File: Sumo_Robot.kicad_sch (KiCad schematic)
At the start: 0 parts

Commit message: updated poer and range sensor scheamtics
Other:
- sheet RangeSensors ports: added SCL, SDA; removed none
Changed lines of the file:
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@@
 	(paper "A4")
 	(sheet
-		(at 39.37 154.94)
+		(at 35.56 176.53)
 		(size 22.86 15.24)
 		(exclude_from_sim no)
@@
 		)
 		(property "Sheetname" "Mechanical"
-			(at 39.37 154.2284 0)
+			(at 35.56 175.8184 0)
 			(effects
 				(font
@@
 		)
 		(property "Sheetfile" "mechanical.kicad_sch"
-			(at 39.37 170.7646 0)
+			(at 35.56 192.3546 0)
 			(effects
 				(font
@@
 	)
 	(sheet
-		(at 223.52 27.94)
+		(at 38.1 137.16)
 		(size 24.13 17.78)
 		(exclude_from_sim no)
@@
 		)
 		(property "Sheetname" "InfraredReceiver"
-			(at 223.52 27.2284 0)
+			(at 38.1 136.4484 0)
 			(effects
 				(font
@@
 		)
 		(property "Sheetfile" "receiver.kicad_sch"
-			(at 223.52 46.3046 0)
+			(at 38.1 155.5246 0)
 			(effects
 				(font
@@
 	)
 	(sheet
-		(at 35.56 68.58)
+		(at 33.02 60.96)
 		(size 27.94 20.32)
 		(exclude_from_sim no)
@@
 		)
 		(property "Sheetname" "RangeSensors"
-			(at 35.56 67.8684 0)
+			(at 33.02 60.2484 0)
 			(effects
 				(font
@@
 		)
 		(property "Sheetfile" "range.kicad_sch"
-			(at 35.56 89.4846 0)
-			(effects
-				(font
-					(size 1.27 1.27)
-				)
-				(justify left top)
-			)
-		)
+			(at 33.02 81.8646 0)
+			(effects
+				(font
+					(size 1.27 1.27)
+				)
+				(justify left top)
+			)
+		)
+		(pin "SCL" input
+			(at 60.96 67.31 0)
+			(effects
+				(font
+					(size 1.27 1.27)
+				)
+				(justify right)
+			)
+		)
+		(pin "SDA" input
+			(at 60.96 73.66 0)
+			(effects
+				(font
+					(size 1.27 1.27)
+				)
+				(justify right)
+			)
+		)

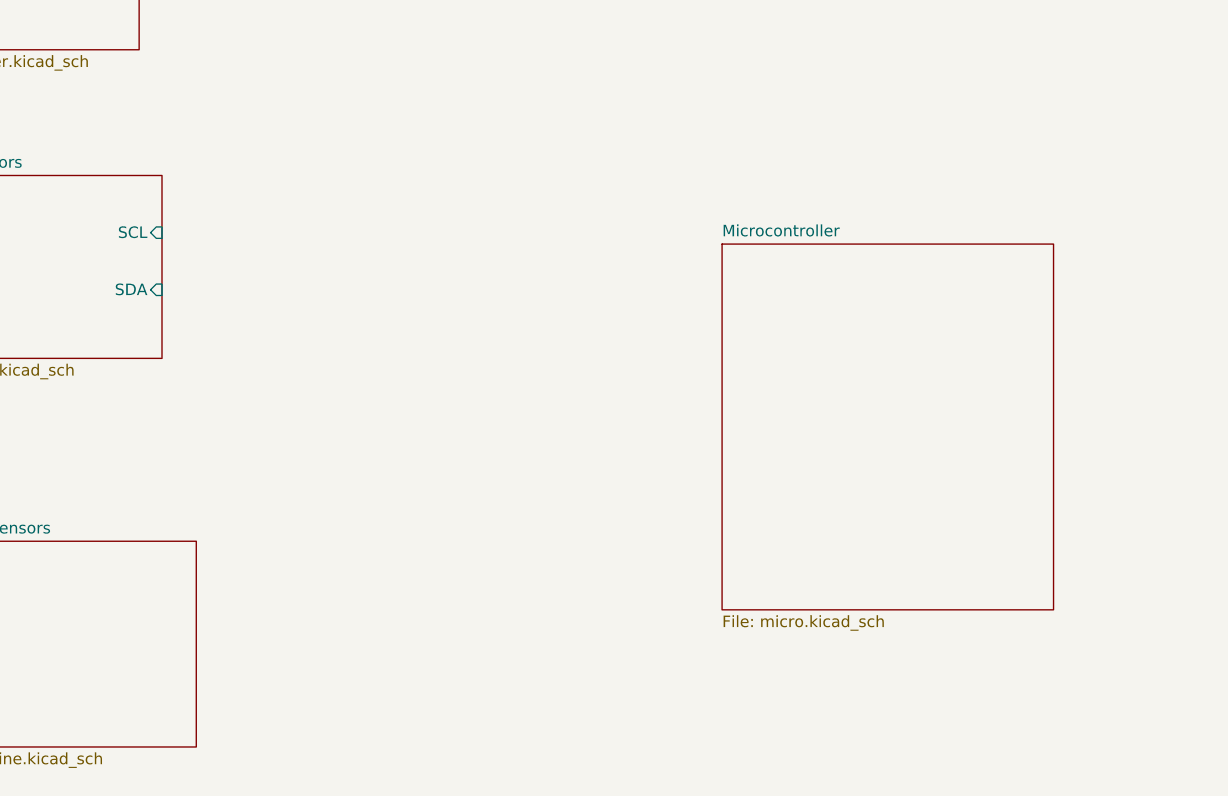
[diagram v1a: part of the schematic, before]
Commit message: added I2C lines
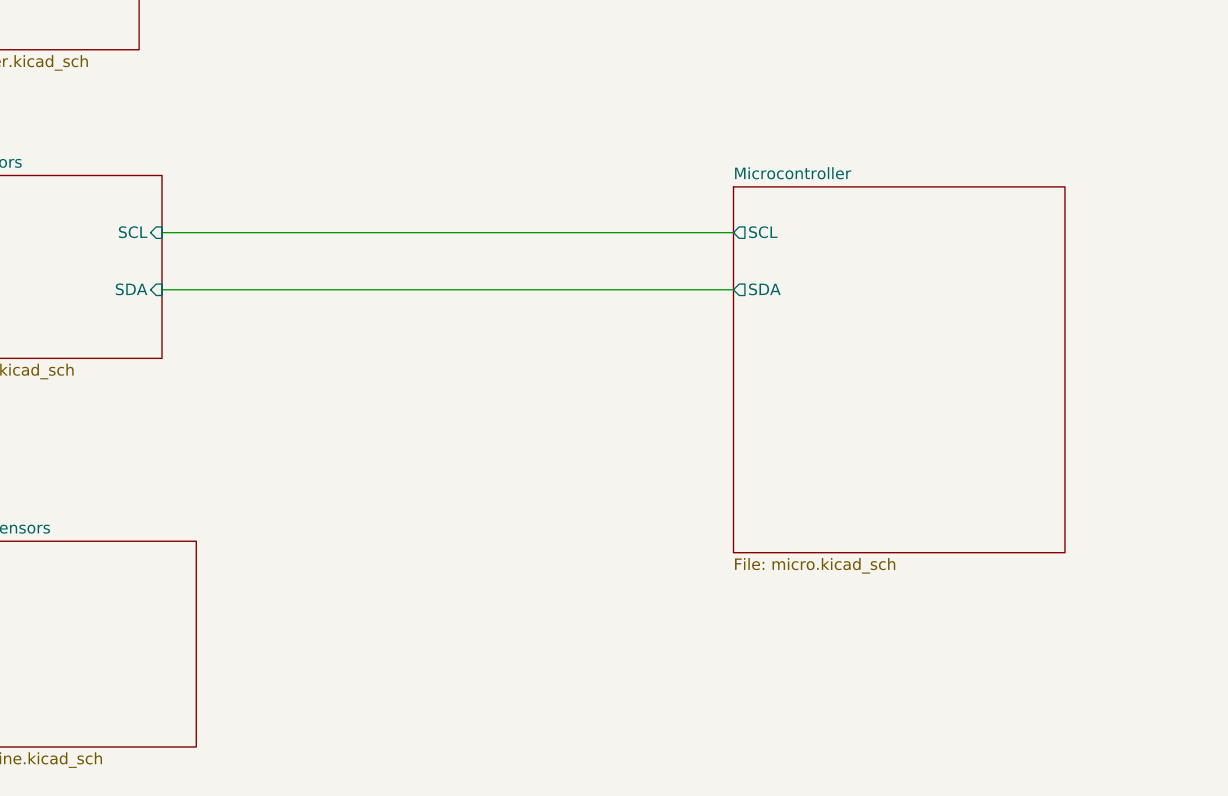
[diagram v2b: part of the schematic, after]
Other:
- sheet Microcontroller ports: added SCL, SDA; removed none
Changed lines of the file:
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@@
 	(generator_version "9.0")
 	(paper "A4")
+	(wire
+		(pts
+			(xy 60.96 67.31) (xy 124.46 67.31)
+		)
+		(stroke
+			(width 0)
+			(type default)
+		)
+	)
+	(wire
+		(pts
+			(xy 60.96 73.66) (xy 124.46 73.66)
+		)
+		(stroke
+			(width 0)
+			(type default)
+		)
+	)
 	(sheet
 		(at 35.56 176.53)
@@
 	)
 	(sheet
-		(at 123.19 68.58)
+		(at 124.46 62.23)
 		(size 36.83 40.64)
 		(exclude_from_sim no)
@@
 		)
 		(property "Sheetname" "Microcontroller"
-			(at 123.19 67.8684 0)
+			(at 124.46 61.5184 0)
 			(effects
 				(font
@@
 		)
 		(property "Sheetfile" "micro.kicad_sch"
-			(at 123.19 109.8046 0)
-			(effects
-				(font
-					(size 1.27 1.27)
-				)
-				(justify left top)
-			)
-		)
+			(at 124.46 103.4546 0)
+			(effects
+				(font
+					(size 1.27 1.27)
+				)
+				(justify left top)
+			)
+		)
+		(pin "SCL" output
+			(at 124.46 67.31 180)
+			(effects
+				(font
+					(size 1.27 1.27)
+				)
+				(justify left)
+			)
+		)
+		(pin "SDA" output
+			(at 124.46 73.66 180)
+			(effects
+				(font
+					(size 1.27 1.27)
+				)
+				(justify left)
+			)
+		)

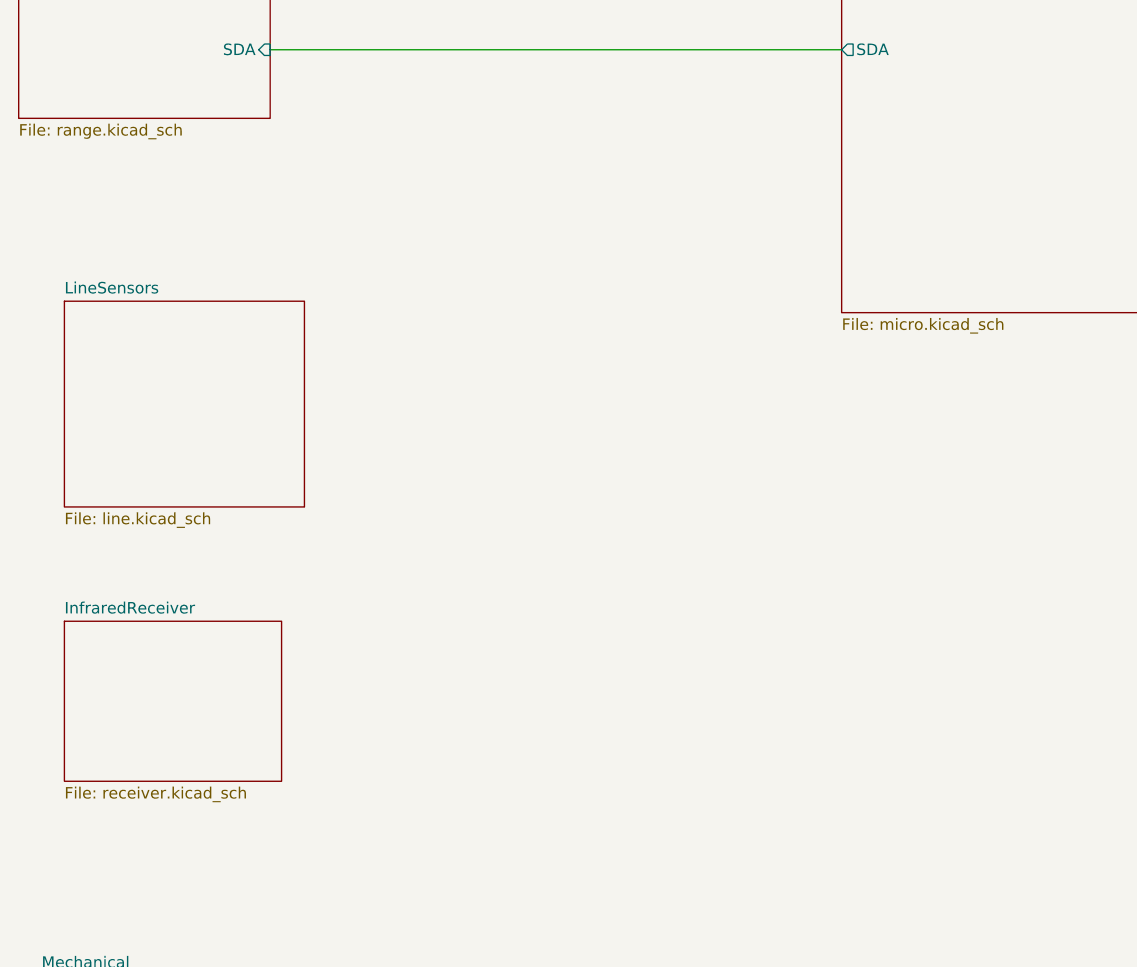
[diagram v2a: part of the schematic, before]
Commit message: added IR receiver circuit
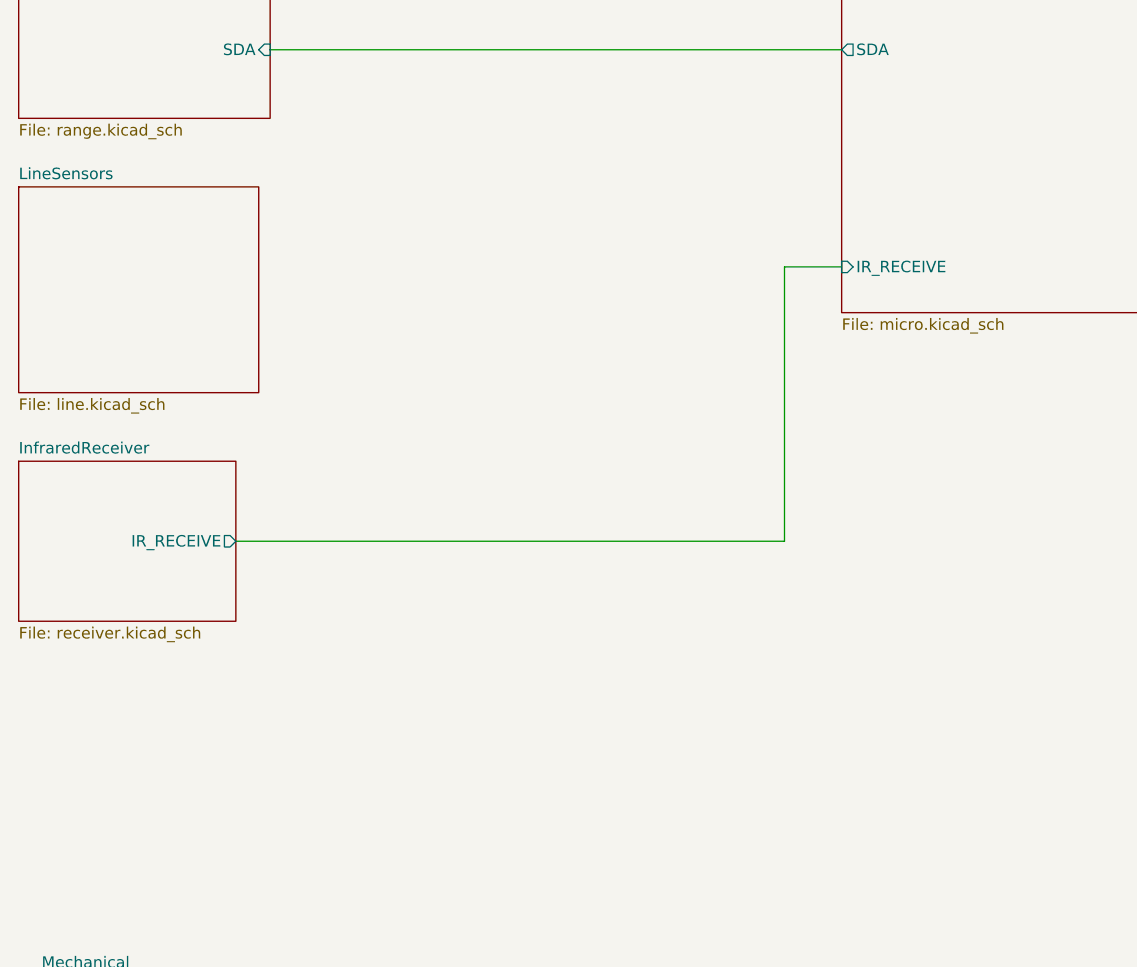
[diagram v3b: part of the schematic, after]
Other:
- sheet InfraredReceiver ports: added IR_RECEIVE; removed none
- sheet Microcontroller ports: added IR_RECEIVE; removed none
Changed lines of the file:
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@@
+	(wire
+		(pts
+			(xy 118.11 128.27) (xy 118.11 97.79)
+		)
+		(stroke
+			(width 0)
+			(type default)
+		)
+	)
+	(wire
+		(pts
+			(xy 57.15 128.27) (xy 118.11 128.27)
+		)
+		(stroke
+			(width 0)
+			(type default)
+		)
+	)
 	(wire
 		(pts
@@
 		)
 	)
+	(wire
+		(pts
+			(xy 118.11 97.79) (xy 124.46 97.79)
+		)
+		(stroke
+			(width 0)
+			(type default)
+		)
+	)
 	(sheet
 		(at 35.56 176.53)
@@
 	)
 	(sheet
-		(at 38.1 137.16)
+		(at 33.02 119.38)
 		(size 24.13 17.78)
 		(exclude_from_sim no)
@@
 		)
 		(property "Sheetname" "InfraredReceiver"
-			(at 38.1 136.4484 0)
+			(at 33.02 118.6684 0)
 			(effects
 				(font
@@
 		)
 		(property "Sheetfile" "receiver.kicad_sch"
-			(at 38.1 155.5246 0)
-			(effects
-				(font
-					(size 1.27 1.27)
-				)
-				(justify left top)
+			(at 33.02 137.7446 0)
+			(effects
+				(font
+					(size 1.27 1.27)
+				)
+				(justify left top)
+			)
+		)
+		(pin "IR_RECEIVE" output
+			(at 57.15 128.27 0)
+			(effects
+				(font
+					(size 1.27 1.27)
+				)
+				(justify right)
 			)
 		)
@@
 			)
 		)
+		(pin "IR_RECEIVE" input
+			(at 124.46 97.79 180)
+			(effects
+				(font
+					(size 1.27 1.27)
+				)
+				(justify left)
+			)
+		)
 		(instances
 			(project "Sumo_Robot"
@@
 	)
 	(sheet
-		(at 38.1 101.6)
+		(at 33.02 88.9)
 		(size 26.67 22.86)
 		(exclude_from_sim no)
@@
 		)
 		(property "Sheetname" "LineSensors"
-			(at 38.1 100.8884 0)
+			(at 33.02 88.1884 0)
 			(effects
 				(font
@@
 		)
 		(property "Sheetfile" "line.kicad_sch"
-			(at 38.1 125.0446 0)
-			(effects
-				(font
+			(at 33.02 112.3446 0)
+			(effects
+				(font

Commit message: added more details to schematics
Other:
- sheet LineSensors ports: added LD_BACK_LEFT, LD_BACK_RIGHT, LD_FRONT_LEFT, LD_FRONT_RIGHT; removed none
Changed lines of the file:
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@@
+			)
+		)
+		(pin "LD_FRONT_LEFT" output
+			(at 59.69 92.71 0)
+			(effects
+				(font
+					(size 1.27 1.27)
+				)
+				(justify right)
+			)
+		)
+		(pin "LD_BACK_RIGHT" output
+			(at 59.69 107.95 0)
+			(effects
+				(font
+					(size 1.27 1.27)
+				)
+				(justify right)
+			)
+		)
+		(pin "LD_BACK_LEFT" output
+			(at 59.69 102.87 0)
+			(effects
+				(font
+					(size 1.27 1.27)
+				)
+				(justify right)
+			)
+		)
+		(pin "LD_FRONT_RIGHT" output
+			(at 59.69 97.79 0)
+			(effects
+				(font
+					(size 1.27 1.27)
+				)
+				(justify right)
 			)
 		)

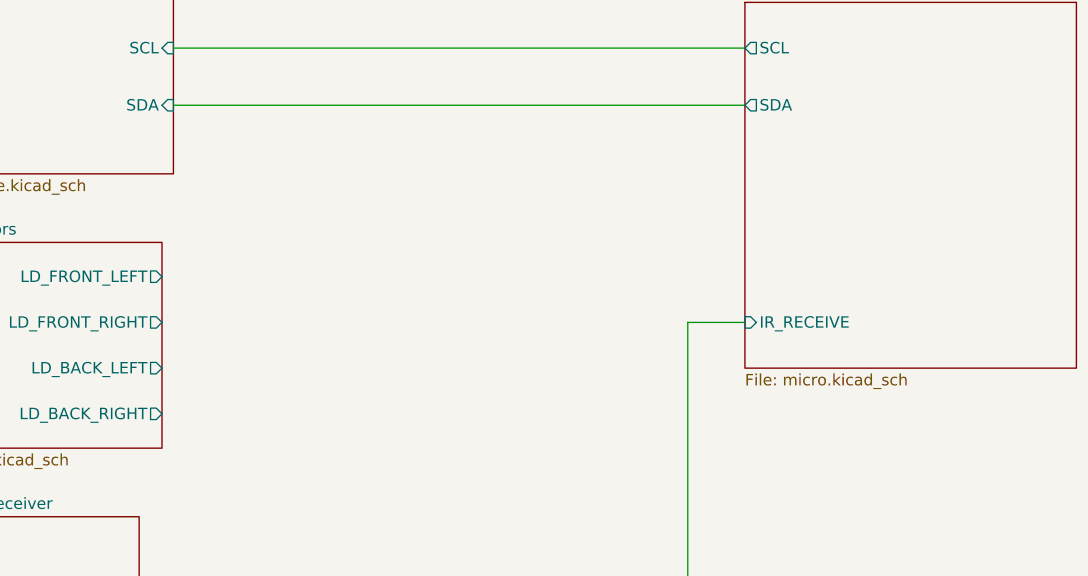
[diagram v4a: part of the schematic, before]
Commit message: updated logic for MCU
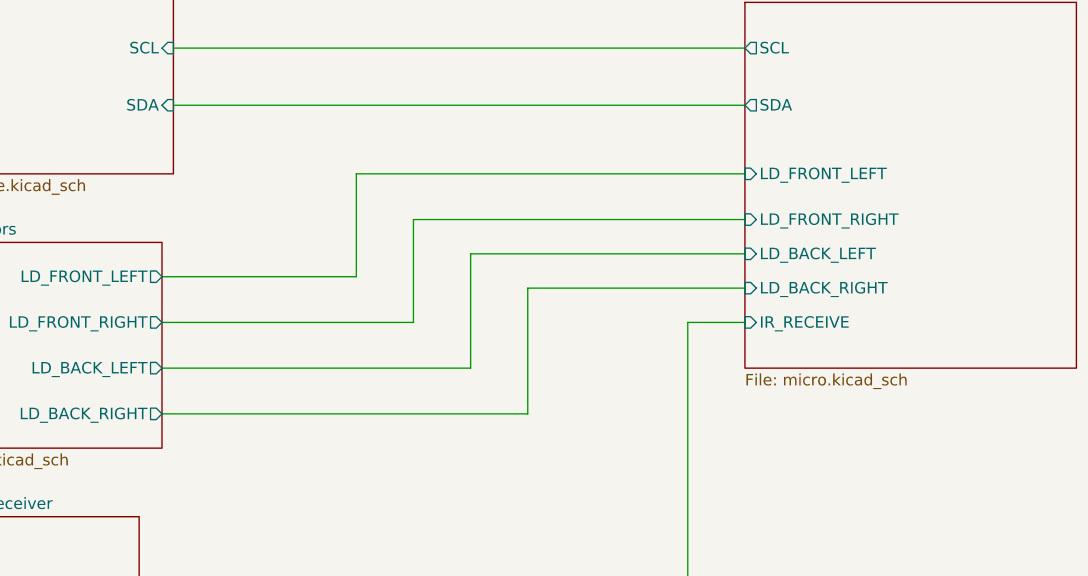
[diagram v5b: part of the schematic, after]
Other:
- sheet Microcontroller ports: added LD_BACK_LEFT, LD_BACK_RIGHT, LD_FRONT_LEFT, LD_FRONT_RIGHT; removed none
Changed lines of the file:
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@@
+	(wire
+		(pts
+			(xy 59.69 92.71) (xy 81.28 92.71)
+		)
+		(stroke
+			(width 0)
+			(type default)
+		)
+	)
+	(wire
+		(pts
+			(xy 81.28 81.28) (xy 124.46 81.28)
+		)
+		(stroke
+			(width 0)
+			(type default)
+		)
+	)
+	(wire
+		(pts
+			(xy 59.69 97.79) (xy 87.63 97.79)
+		)
+		(stroke
+			(width 0)
+			(type default)
+		)
+	)
+	(wire
+		(pts
+			(xy 93.98 102.87) (xy 93.98 90.17)
+		)
+		(stroke
+			(width 0)
+			(type default)
+		)
+	)
+	(wire
+		(pts
+			(xy 100.33 93.98) (xy 124.46 93.98)
+		)
+		(stroke
+			(width 0)
+			(type default)
+		)
+	)
 	(wire
 		(pts
@@
 	(wire
 		(pts
+			(xy 100.33 107.95) (xy 100.33 93.98)
+		)
+		(stroke
+			(width 0)
+			(type default)
+		)
+	)
+	(wire
+		(pts
+			(xy 93.98 90.17) (xy 124.46 90.17)
+		)
+		(stroke
+			(width 0)
+			(type default)
+		)
+	)
+	(wire
+		(pts
+			(xy 81.28 92.71) (xy 81.28 81.28)
+		)
+		(stroke
+			(width 0)
+			(type default)
+		)
+	)
+	(wire
+		(pts
+			(xy 59.69 107.95) (xy 100.33 107.95)
+		)
+		(stroke
+			(width 0)
+			(type default)
+		)
+	)
+	(wire
+		(pts
+			(xy 59.69 102.87) (xy 93.98 102.87)
+		)
+		(stroke
+			(width 0)
+			(type default)
+		)
+	)
+	(wire
+		(pts
 			(xy 57.15 128.27) (xy 118.11 128.27)
 		)
@@
 	(wire
 		(pts
+			(xy 87.63 86.36) (xy 124.46 86.36)
+		)
+		(stroke
+			(width 0)
+			(type default)
+		)
+	)
+	(wire
+		(pts
 			(xy 118.11 97.79) (xy 124.46 97.79)
+		)
+		(stroke
+			(width 0)
+			(type default)
+		)
+	)
+	(wire
+		(pts
+			(xy 87.63 97.79) (xy 87.63 86.36)
 		)
 		(stroke
@@
 			(effects
 				(font
+					(size 1.27 1.27)
+				)
+				(justify left)
+			)
+		)
+		(pin "LD_BACK_LEFT" input
+			(at 124.46 90.17 180)
+			(effects
+				(font
+					(size 1.27 1.27)
+				)
+				(justify left)
+			)
+		)
+		(pin "LD_BACK_RIGHT" input
+			(at 124.46 93.98 180)
+			(effects
+				(font
+					(size 1.27 1.27)
+				)
+				(justify left)
+			)
+		)
+		(pin "LD_FRONT_LEFT" input
+			(at 124.46 81.28 180)
+			(effects
+				(font
+					(size 1.27 1.27)
+				)
+				(justify left)
+			)
+		)
+		(pin "LD_FRONT_RIGHT" input
+			(at 124.46 86.36 180)
+			(effects
+				(font
